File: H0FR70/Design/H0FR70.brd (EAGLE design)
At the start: 34.6 x 30 mm, 38 parts, among them P2 HEXABIT_17.32_NO_P6_P7_P12, Q1 BSS123, Q2 STD36P4LLF6, U2 INA199A2DCKT, X1 XTALL_CSTCE8M00G52

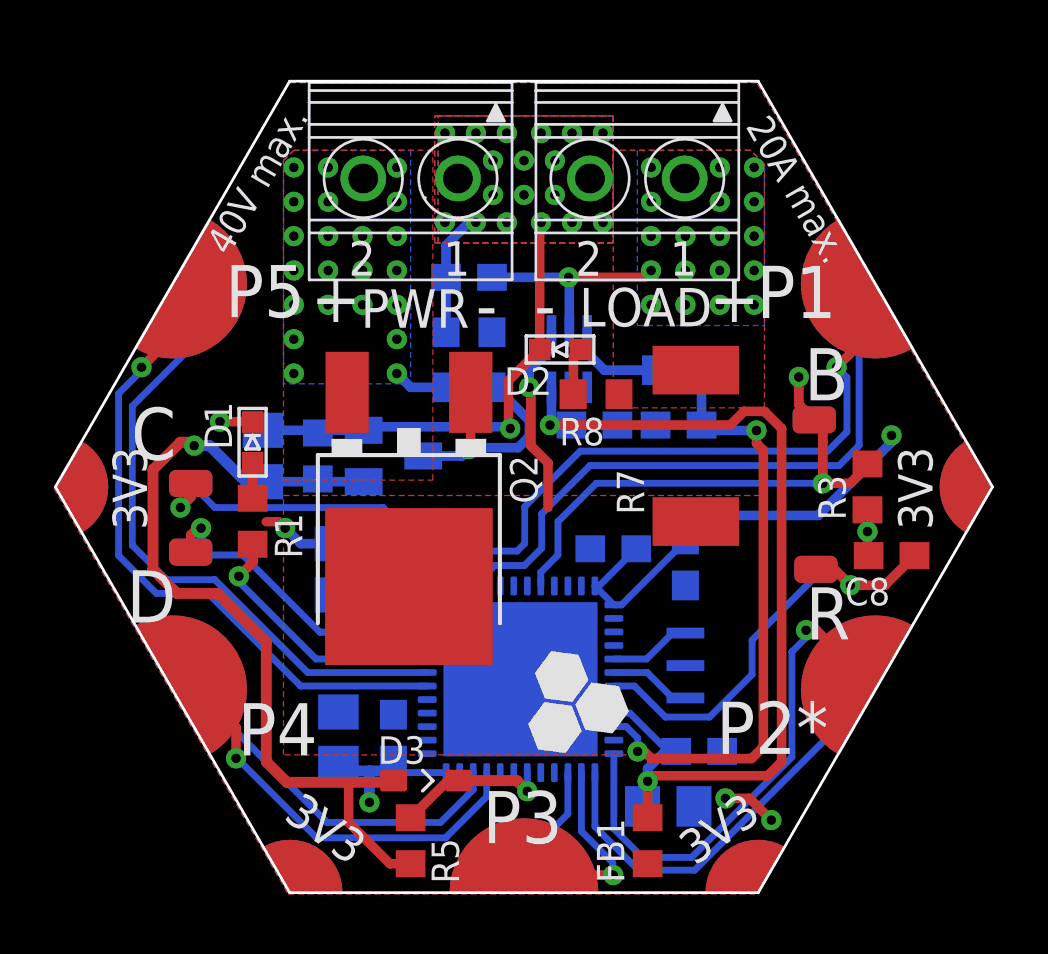
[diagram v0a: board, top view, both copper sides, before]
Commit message: changing power connector to PTR500 (AK500/3) adding voltage diveder at the gate of power transistor (4.7/14.7)
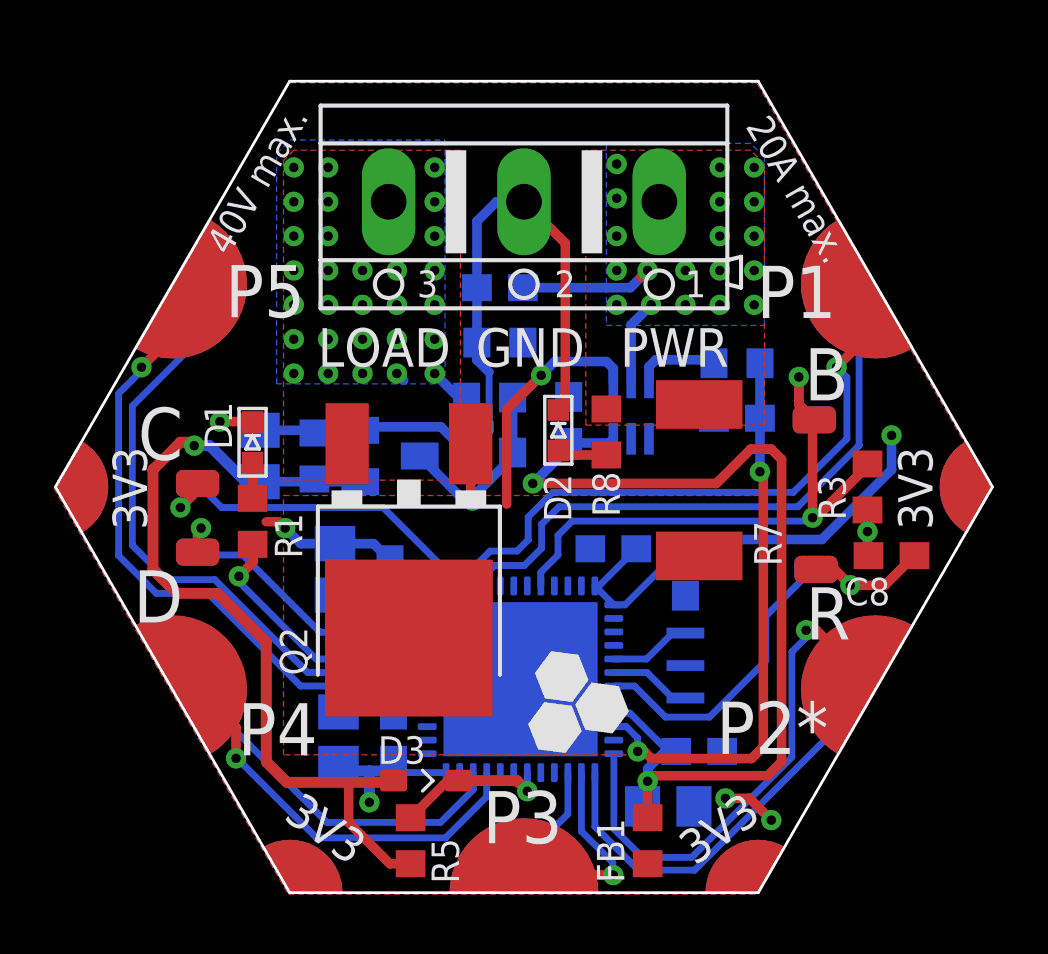
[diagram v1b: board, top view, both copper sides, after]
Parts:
- removed LOAD, PWR: CON-PHOENIX-350_1751248, Hexabitz:CON-PHOENIX-350_1751248
- added R9: 4.7K, Hexabitz:R-0603
- added X2: (no value), con-ptr500:AK500/3
- R4: value 4.7K -> 10K
- moved D2 2.99 mm to (35.9, 36.8), turned to 180 degrees
- moved U2 2.98 mm to (38.6, 37.5)
- moved R10 2.17 mm to (42.5, 39.2)
- moved C13 2.17 mm to (42.5, 37.2)
- moved Q2 1.91 mm to (30.4, 29.1)
- moved R8 1.45 mm to (37.7, 36.7), turned to 90 degrees
- moved R7 1.28 mm to (41.1, 34.9)
- moved C12 1.20 mm to (33.8, 42.0)
- moved R2 1.20 mm to (33.8, 40.0)
- moved C11 0.97 mm to (36.3, 37.1), turned to 90 degrees
- moved R4 0.85 mm to (33.4, 38.0)
- moved C6 0.38 mm to (40.6, 31.5)
- moved C 0.25 mm to (22.6, 34.8)
- moved D 0.25 mm to (22.6, 32.3)
- moved C10 0.13 mm to (24.9, 35.8)
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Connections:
- net +LOAD: now also X2.1; no longer LOAD.1
- net AGND: now also R9.1, X2.2; no longer LOAD.2, PWR.1
- net N$7: now also R9.2
- net V_LOAD: now also X2.3; no longer PWR.2
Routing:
- net AGND: track 22.3 -> 27.7 mm, vias 19 -> 0
- net CURRENT_SENSE: track 22.4 -> 20.8 mm
- net S: track 7.16 -> 8.79 mm
- net VDDA: track 35.5 -> 36.8 mm
- net B1: track 21.1 -> 22.0 mm
- net N$1: track 12.4 -> 11.6 mm
- net VDD: track 29.4 -> 29.9 mm
- net V_LOAD: track 2.39 -> 1.91 mm, vias 22 -> 29
- removed copper zone on layer 1, net AGND
- removed copper zone on layer 16, net AGND
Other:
- board text added: "LOAD"
- board text added: "PWR"
- board text removed: "+"
- board text removed: "-"

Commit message: adding: zenar at gate + 0R res
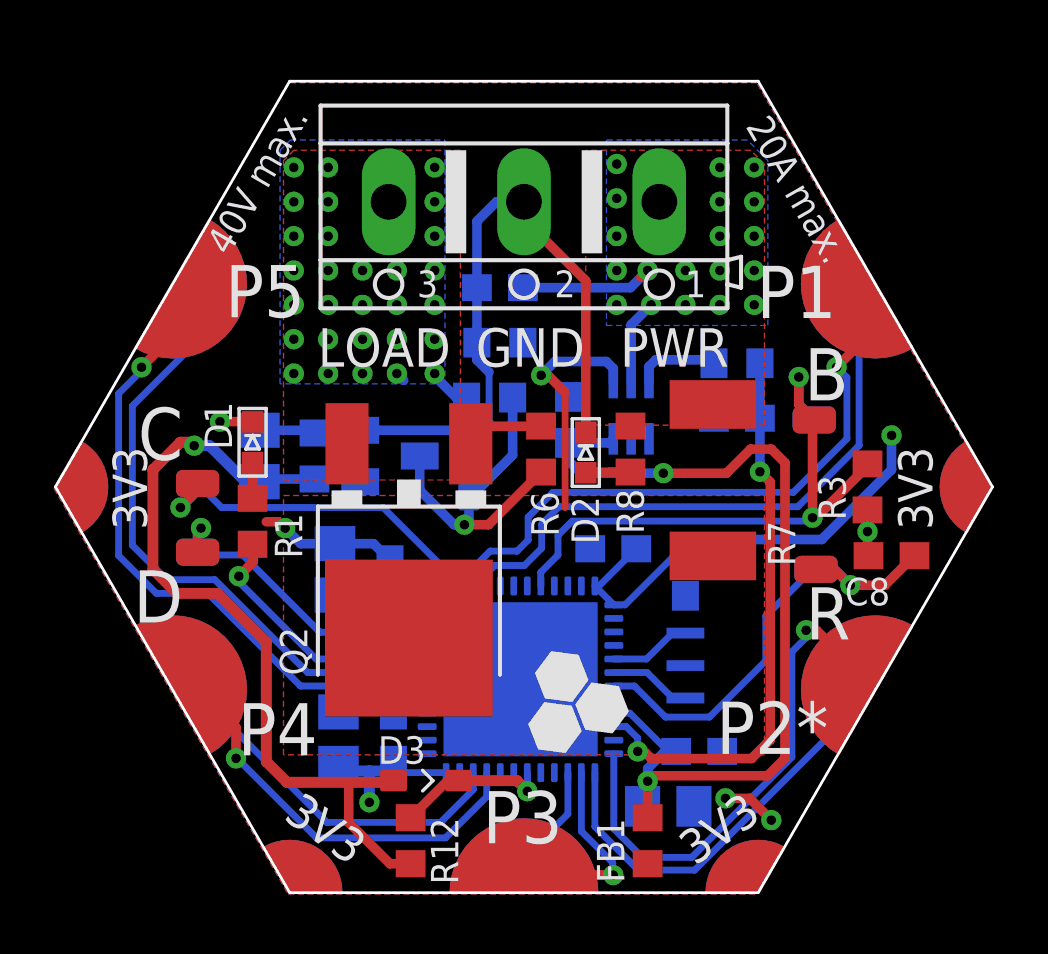
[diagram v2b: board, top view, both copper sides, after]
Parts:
- removed R9: 4.7K, Hexabitz:R-0603
- added D4: BZT52C2V0S-7-F, Hexabitz:SOD-323
- added R12: 10.0K, Hexabitz:R-0603
- R4: value 10K -> 10.0K
- R5: value (none) -> 680K
- R6: value (none) -> 0.0R
- moved R5 14.7 mm to (26.9, 35.8), flipped to the bottom
- moved R6 8.39 mm to (35.3, 36.1), flipped to the top
- moved D2 1.31 mm to (37.0, 35.9)
- moved R8 1.09 mm to (38.6, 36.1)
- moved R7 0.51 mm to (41.7, 34.9)
- turned R4 to 180 degrees
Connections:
- new net N$10: Q2.1, R6.1
- net AGND: now also D4.+, R5.1; no longer R6.1, R9.1
- net EN_PIN: now also R12.2; no longer R5.1
- net N$13: now also R12.1; no longer R6.2
- net N$7: now also D4.-, R4.2, R6.2; no longer Q2.1, R4.1, R9.2
- net V_LOAD: now also R4.1; no longer R4.2
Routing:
- net N$7: track 9.22 -> 12.6 mm
- net N$10: track 0.00 -> 2.87 mm
- net VDDA: track 36.8 -> 34.2 mm
